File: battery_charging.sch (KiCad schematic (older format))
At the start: 4 parts

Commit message: annotate schematic
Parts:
- gave numbers to parts that had none: 4
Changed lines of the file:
@@
 VBAT
 $Comp
-L Battery_Management:MCP73831-2-OT U?
+L Battery_Management:MCP73831-2-OT U8
 U 1 1 5C91A071
 P 3200 2000
-F 0 "U?" H 3200 2481 50  0000 C CNN
+F 0 "U8" H 3200 2481 50  0000 C CNN
 F 1 "MCP73831-2-OT" H 3200 2390 50  0000 C CNN
 F 2 "Package_TO_SOT_SMD:SOT-23-5" H 3250 1750 50  0001 L CIN
@@
 	3600 2100 4000 2100
 $Comp
-L Device:R_Small_US R?
+L Device:R_Small_US R15
 U 1 1 5C91CC9C
 P 4000 1900
-F 0 "R?" H 4068 1946 50  0000 L CNN
+F 0 "R15" H 4068 1946 50  0000 L CNN
 F 1 "10k" H 4068 1855 50  0000 L CNN
 F 2 "" H 4000 1900 50  0001 C CNN
@@
 Connection ~ 3200 1650
 $Comp
-L Device:R_Small_US R?
+L Device:R_Small_US R14
 U 1 1 5C91D6DA
 P 2750 2300
-F 0 "R?" H 2818 2346 50  0000 L CNN
+F 0 "R14" H 2818 2346 50  0000 L CNN
 F 1 "1k" H 2818 2255 50  0000 L CNN
 F 2 "" H 2750 2300 50  0001 C CNN
@@
 	3200 2500 3200 2300
 $Comp
-L Device:C_Small C?
+L Device:C_Small C13
 U 1 1 5C91EAAB
 P 2600 1900
-F 0 "C?" H 2692 1946 50  0000 L CNN
+F 0 "C13" H 2692 1946 50  0000 L CNN
 F 1 "10uF" H 2692 1855 50  0000 L CNN
 F 2 "" H 2600 1900 50  0001 C CNN

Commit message: reannotate schematic
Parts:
- renumbered R14 to R15, R15 to R16
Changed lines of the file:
@@
 	3600 2100 4000 2100
 $Comp
-L Device:R_Small_US R15
+L Device:R_Small_US R16
 U 1 1 5C91CC9C
 P 4000 1900
-F 0 "R15" H 4068 1946 50  0000 L CNN
+F 0 "R16" H 4068 1946 50  0000 L CNN
 F 1 "10k" H 4068 1855 50  0000 L CNN
 F 2 "" H 4000 1900 50  0001 C CNN
@@
 Connection ~ 3200 1650
 $Comp
-L Device:R_Small_US R14
+L Device:R_Small_US R15
 U 1 1 5C91D6DA
 P 2750 2300
-F 0 "R14" H 2818 2346 50  0000 L CNN
+F 0 "R15" H 2818 2346 50  0000 L CNN
 F 1 "1k" H 2818 2255 50  0000 L CNN
 F 2 "" H 2750 2300 50  0001 C CNN

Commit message: associate footprints with all parts
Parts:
- C13: footprint (none) -> Capacitor_SMD:C_0603_1608Metric_Pad1.05x0.95mm_HandSolder
- R15, R16: footprint (none) -> Resistor_SMD:R_0603_1608Metric_Pad1.05x0.95mm_HandSolder
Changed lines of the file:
@@
 F 0 "R16" H 4068 1946 50  0000 L CNN
 F 1 "10k" H 4068 1855 50  0000 L CNN
-F 2 "" H 4000 1900 50  0001 C CNN
+F 2 "Resistor_SMD:R_0603_1608Metric_Pad1.05x0.95mm_HandSolder" H 4000 1900 50  0001 C CNN
 F 3 "~" H 4000 1900 50  0001 C CNN
 	1    4000 1900
@@
 F 0 "R15" H 2818 2346 50  0000 L CNN
 F 1 "1k" H 2818 2255 50  0000 L CNN
-F 2 "" H 2750 2300 50  0001 C CNN
+F 2 "Resistor_SMD:R_0603_1608Metric_Pad1.05x0.95mm_HandSolder" H 2750 2300 50  0001 C CNN
 F 3 "~" H 2750 2300 50  0001 C CNN
 	1    2750 2300
@@
 F 0 "C13" H 2692 1946 50  0000 L CNN
 F 1 "10uF" H 2692 1855 50  0000 L CNN
-F 2 "" H 2600 1900 50  0001 C CNN
+F 2 "Capacitor_SMD:C_0603_1608Metric_Pad1.05x0.95mm_HandSolder" H 2600 1900 50  0001 C CNN
 F 3 "~" H 2600 1900 50  0001 C CNN
 	1    2600 1900

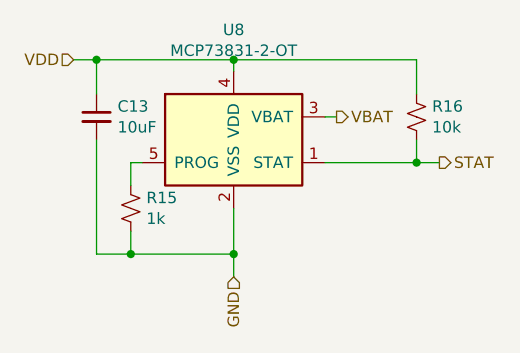
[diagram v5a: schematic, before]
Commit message: switch programming resistor on lipo charger because it apparently maxes at 500 mA current
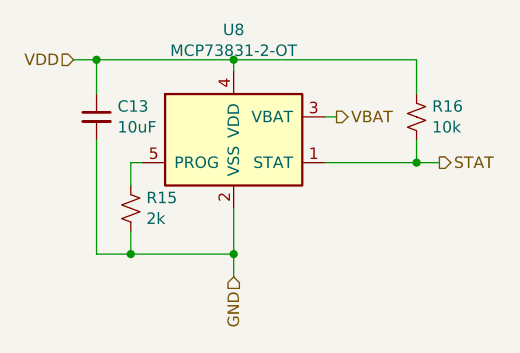
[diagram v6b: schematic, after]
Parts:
- R15: value 1k -> 2k
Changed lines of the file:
@@
 P 2750 2300
 F 0 "R15" H 2818 2346 50  0000 L CNN
-F 1 "1k" H 2818 2255 50  0000 L CNN
+F 1 "2k" H 2818 2255 50  0000 L CNN
 F 2 "Resistor_SMD:R_0603_1608Metric_Pad1.05x0.95mm_HandSolder" H 2750 2300 50  0001 C CNN
 F 3 "~" H 2750 2300 50  0001 C CNN
